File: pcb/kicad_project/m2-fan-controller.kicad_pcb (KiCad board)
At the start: 2 copper layers, 22 x 30 mm, 17 parts, among them J1 Bus_M.2_Socket_E, J2 Conn_01x04, J3 Conn_01x04, J4 JST PH_S2B-PH-K, U1 STM32F042F6P6

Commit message: Hopefully final revision
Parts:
- added TP1: TestPoint, TestPoint:TestPoint_Pad_D1.0mm, F.Cu at (138.5, 105.2)
- moved JP1 1.65 mm to (137.4, 86.5), turned to 180 degrees
- moved C1 0.41 mm to (144.5, 103.4)
- turned R7 to 0 degrees
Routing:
- net +3.3V: track 0.00 -> 40.5 mm, vias 0 -> 6
- net BOOT0: track 4.47 -> 21.7 mm
- net RST: track 0.00 -> 16.2 mm, vias 0 -> 2
- net TACH_1: track 0.00 -> 12.9 mm, vias 0 -> 2
- net TACH_0: track 0.00 -> 11.4 mm
- net PWM_0: track 0.00 -> 8.10 mm
- net PWM_1: track 0.00 -> 6.81 mm
- net Net-(J1-~{PERST0}): track 0.00 -> 5.77 mm, vias 0 -> 1
- net +12V: track 31.4 -> 27.5 mm
- net GND: track 0.00 -> 1.50 mm, vias 0 -> 4
- added copper zone on B.Cu, net +3.3V
- added copper zone on B.Cu, net GND
- added copper zone on F.Cu, net GND
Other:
- board text added: "(c) 2026 - Sergio Carmine"
- board text added: "3.3V"
- board text added: "M.2 fan controller"

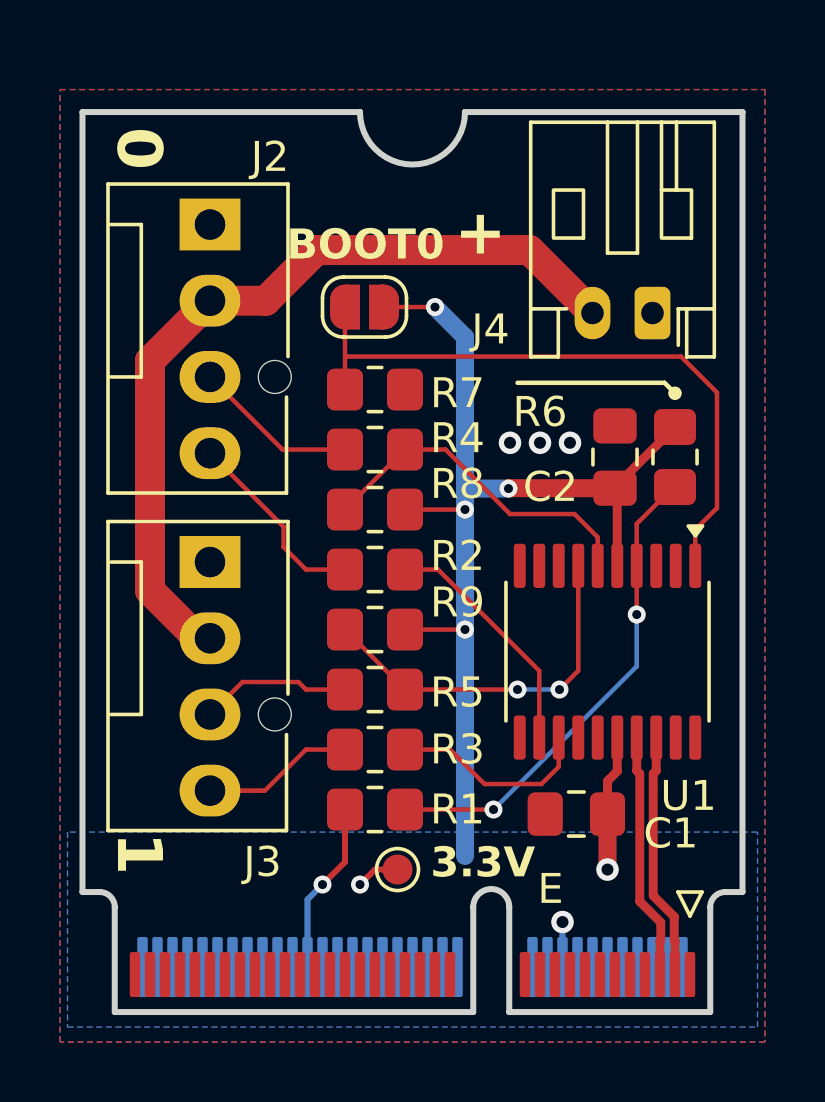
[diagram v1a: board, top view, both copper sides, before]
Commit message: Add debug header
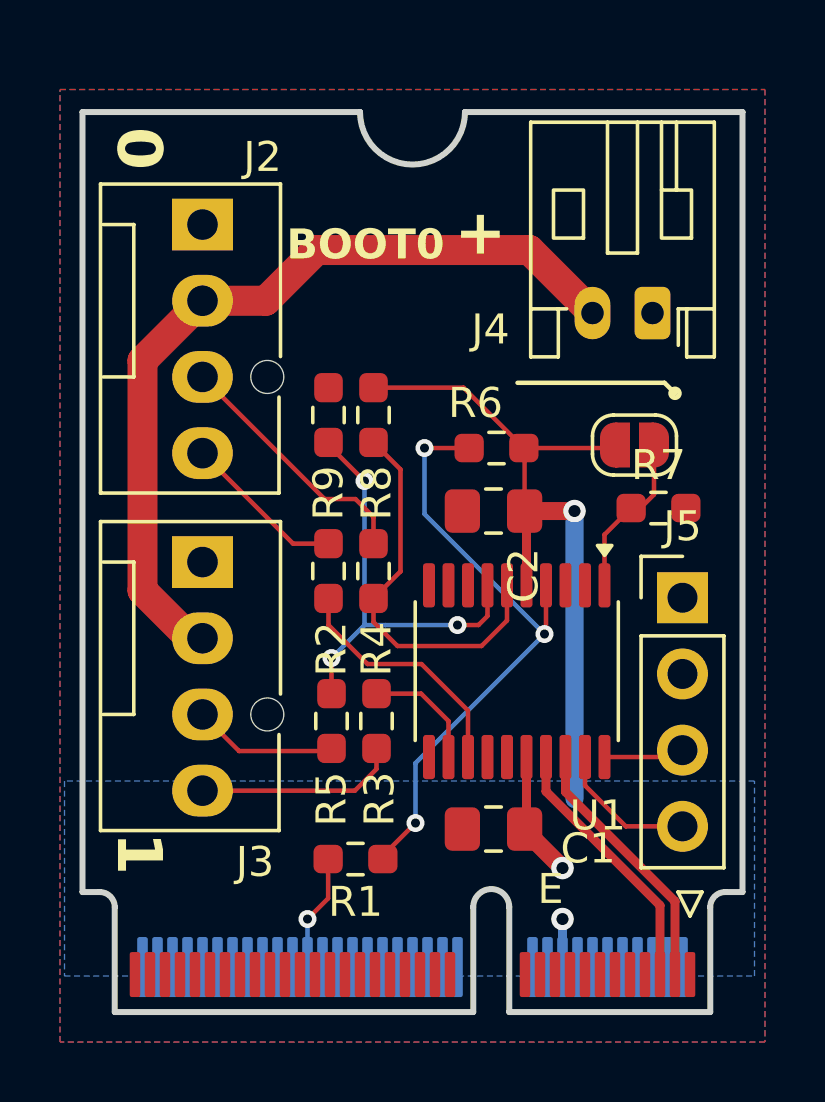
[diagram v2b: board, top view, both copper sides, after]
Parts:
- removed TP1: TestPoint, TestPoint:TestPoint_Pad_D1.0mm
- added J5: Conn_02x02_Odd_Even, Connector_PinHeader_2.54mm:PinHeader_1x04_P2.54mm_Vertical, F.Cu at (148.0, 96.2)
- R1, R2, R3, R4, R5, R6, R7, R8, R9: footprint Resistor_SMD:R_0805_2012Metric_Pad1.20x1.40mm_HandSolder -> Resistor_SMD:R_0603_1608Metric_Pad0.98x0.95mm_HandSolder
- moved R7 10.2 mm to (147.2, 93.2)
- moved JP1 10.1 mm to (146.4, 91.1), turned to 0 degrees
- moved R9 7.32 mm to (136.2, 90.1), turned to -90 degrees
- moved R6 5.96 mm to (141.8, 91.2), turned to 180 degrees
- moved C2 4.43 mm to (141.7, 93.3), turned to 180 degrees
- moved R4 4.05 mm to (137.7, 95.3), turned to 90 degrees
- moved R8 3.15 mm to (137.7, 90.1), turned to -90 degrees
- moved U1 3.09 mm to (142.5, 98.6)
- moved C1 2.81 mm to (141.7, 103.9)
- moved R5 1.79 mm to (136.3, 100.3), turned to -90 degrees
- moved R1 1.77 mm to (137.1, 104.9)
- moved R2 1.55 mm to (136.2, 95.3), turned to 90 degrees
- moved R3 0.95 mm to (137.8, 100.3), turned to -90 degrees
- moved J2 0.25 mm to (132.0, 83.8)
- moved J3 0.25 mm to (132.0, 95.0)
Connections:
- U1 pad 12: PWM_0 -> PWM_1
- U1 pad 13: PWM_1 -> PWM_0
- U1 pad 19: unconnected-(U1-PA13-Pad19) -> SWDIO
- U1 pad 20: unconnected-(U1-PA14-Pad20) -> SWCLK
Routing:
- net BOOT0: track 21.7 -> 5.94 mm
- net +3.3V: track 40.5 -> 29.1 mm, vias 6 -> 2
- net SWDIO: track 0.00 -> 4.76 mm
- net RST: track 16.2 -> 20.5 mm, vias 2 -> 3
- net Net-(J2-Pin_3): track 5.50 -> 8.55 mm
- net PWM_1: track 6.81 -> 3.98 mm
- net SWCLK: track 0.00 -> 2.70 mm
- net Net-(J1-~{PERST0}): track 5.77 -> 3.88 mm
- net TACH_1: track 12.9 -> 14.6 mm, vias 2 -> 3
- net Net-(J3-Pin_4): track 5.07 -> 6.79 mm
- net TACH_0: track 11.4 -> 13.0 mm
- net Net-(J2-Pin_4): track 6.51 -> 5.45 mm
- net Net-(J3-Pin_3): track 5.05 -> 4.31 mm
- net USB_D-: track 8.24 -> 8.82 mm
- net USB_D+: track 8.24 -> 8.76 mm
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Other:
- board text removed: "3.3V"

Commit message: Final revision
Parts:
- removed JP1: Jumper_2_Open, Jumper:SolderJumper-2_P1.3mm_Open_RoundedPad1.0x1.5mm
- added C3: 0.1uF, Capacitor_SMD:C_0805_2012Metric_Pad1.18x1.45mm_HandSolder, F.Cu at (136.6, 88.3)
- added C4: 0.1uF, Capacitor_SMD:C_0805_2012Metric_Pad1.18x1.45mm_HandSolder, F.Cu at (136.6, 93.9)
- added C5: 1uF, Capacitor_SMD:C_1206_3216Metric, F.Cu at (142.2, 88.8)
- added C6: 1uF, Capacitor_SMD:C_1206_3216Metric, F.Cu at (142.2, 91.2)
- added R10: 10kOhm, Resistor_SMD:R_0603_1608Metric_Pad0.98x0.95mm_HandSolder, F.Cu at (140.2, 103.0)
- added R11: 10kOhm, Resistor_SMD:R_0603_1608Metric_Pad0.98x0.95mm_HandSolder, F.Cu at (138.6, 103.0)
- added U2: TPS22810DBV, Package_TO_SOT_SMD:SOT-23-6, F.Cu at (136.7, 85.6)
- added U3: TPS22810DBV, Package_TO_SOT_SMD:SOT-23-6, F.Cu at (136.7, 91.2)
- C1, C2: footprint Capacitor_SMD:C_0805_2012Metric_Pad1.18x1.45mm_HandSolder -> Capacitor_SMD:C_0603_1608Metric_Pad1.08x0.95mm_HandSolder
- J2, J3: value Conn_01x04 -> JST PH_B4B-PH-K; footprint Connector:FanPinHeader_1x04_P2.54mm_Vertical -> Connector_JST:JST_PH_B4B-PH-K_1x04_P2.00mm_Vertical
- J4: footprint Connector_JST:JST_PH_S2B-PH-K_1x02_P2.00mm_Horizontal -> Connector_JST:JST_PH_B2B-PH-K_1x02_P2.00mm_Vertical
- J5: footprint Connector_PinHeader_2.54mm:PinHeader_1x04_P2.54mm_Vertical -> Connector_PinHeader_1.27mm:PinHeader_1x05_P1.27mm_Vertical
- moved R8 13.1 mm to (135.4, 103.0), turned to 90 degrees
- moved R9 12.9 mm to (137.0, 103.0), turned to 90 degrees
- moved J5 7.00 mm to (148.1, 89.2)
- moved J2 6.80 mm to (130.6, 90.4), turned to 90 degrees
- moved J3 6.55 mm to (130.6, 101.4), turned to 90 degrees
- moved R7 5.15 mm to (145.5, 88.3), turned to 90 degrees
- moved R5 4.75 mm to (140.2, 97.6), turned to 90 degrees
- moved J4 4.38 mm to (145.1, 82.8), turned to 0 degrees
- moved R1 4.35 mm to (132.8, 104.9)
- moved R6 3.87 mm to (145.5, 92.3), turned to -90 degrees
- moved R3 3.62 mm to (135.4, 97.6), turned to 90 degrees
- moved U1 3.18 mm to (145.4, 99.9)
- moved C1 3.00 mm to (144.6, 104.8)
- moved C2 2.62 mm to (143.6, 95.1)
- moved R4 2.46 mm to (138.6, 97.6)
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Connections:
- J2 pad 2: +12V -> Net-(J2-Pin_2)
- J3 pad 2: +12V -> Net-(J3-Pin_2)
- J5 pad 2: +3.3V -> SWCLK
- J5 pad 3: SWCLK -> SWDIO
- J5 pad 4: SWDIO -> BOOT0
- U1 pad 8: unconnected-(U1-PA2-Pad8) -> EN_0
- U1 pad 9: unconnected-(U1-PA3-Pad9) -> EN_1
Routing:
- net EN_0: track 0.00 -> 24.8 mm, vias 0 -> 3
- net EN_1: track 0.00 -> 19.4 mm, vias 0 -> 3
- net Net-(J2-Pin_4): track 5.45 -> 17.2 mm, vias 0 -> 1
- net Net-(J3-Pin_2): track 0.00 -> 11.2 mm
- net SWCLK: track 2.70 -> 13.4 mm, vias 0 -> 1
- net Net-(J2-Pin_3): track 8.55 -> 17.1 mm, vias 0 -> 1
- net +12V: track 27.6 -> 19.9 mm
- net Net-(J2-Pin_2): track 0.00 -> 7.45 mm
- net SWDIO: track 4.76 -> 12.0 mm, vias 0 -> 1
- net PWM_1: track 3.98 -> 11.1 mm
- net GND: track 1.60 -> 7.94 mm, vias 1 -> 11
- net Net-(J3-Pin_3): track 4.31 -> 10.1 mm, vias 0 -> 1
- net BOOT0: track 5.94 -> 10.0 mm
- net Net-(J1-~{PERST0}): track 3.88 -> 6.62 mm
- net USB_D-: track 8.82 -> 6.34 mm
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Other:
- board text added: "12V"
- board text added: "3.3V"
- board text added: "G"
- board text added: "GND"
- board text added: "PCB thickness 0.8 mm"
- board text added: "PWM"
- board text added: "SWCLK"
- board text added: "SWDIO"
- board text added: "TACH"
- board text removed: "+"
- board text removed: "M.2 fan controller"

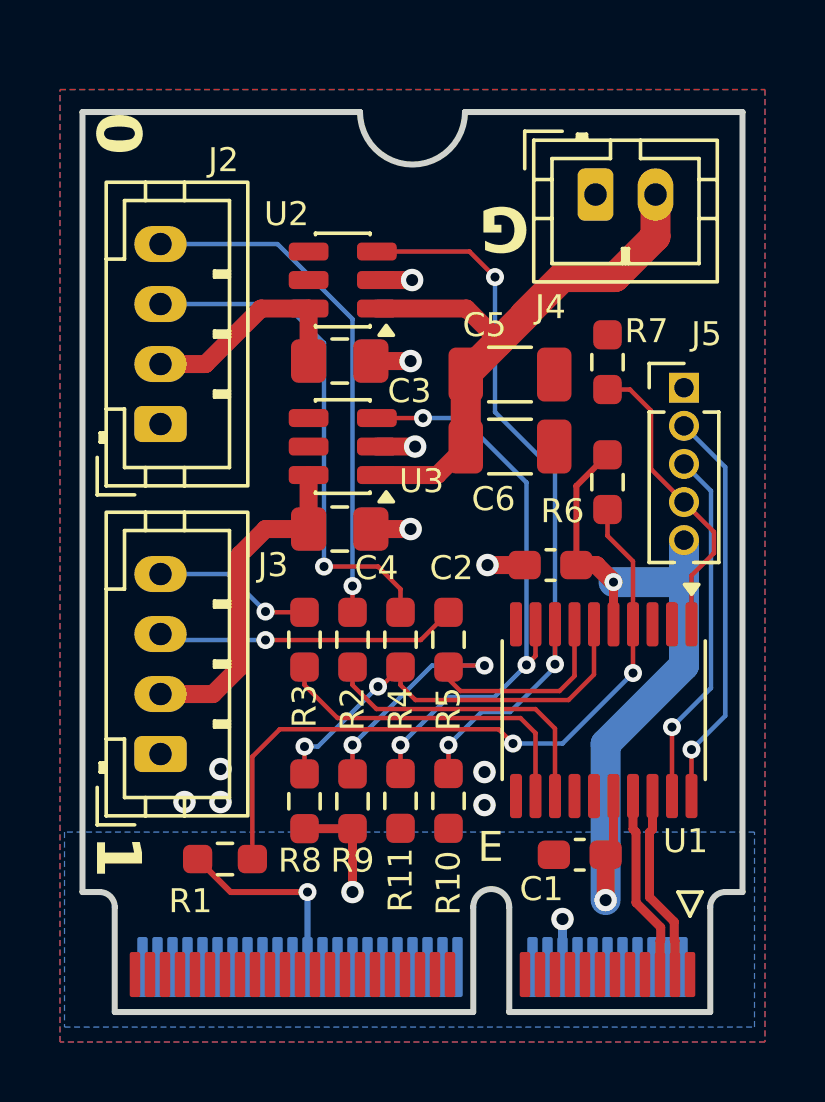
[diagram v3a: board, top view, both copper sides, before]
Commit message: Use 0603 components
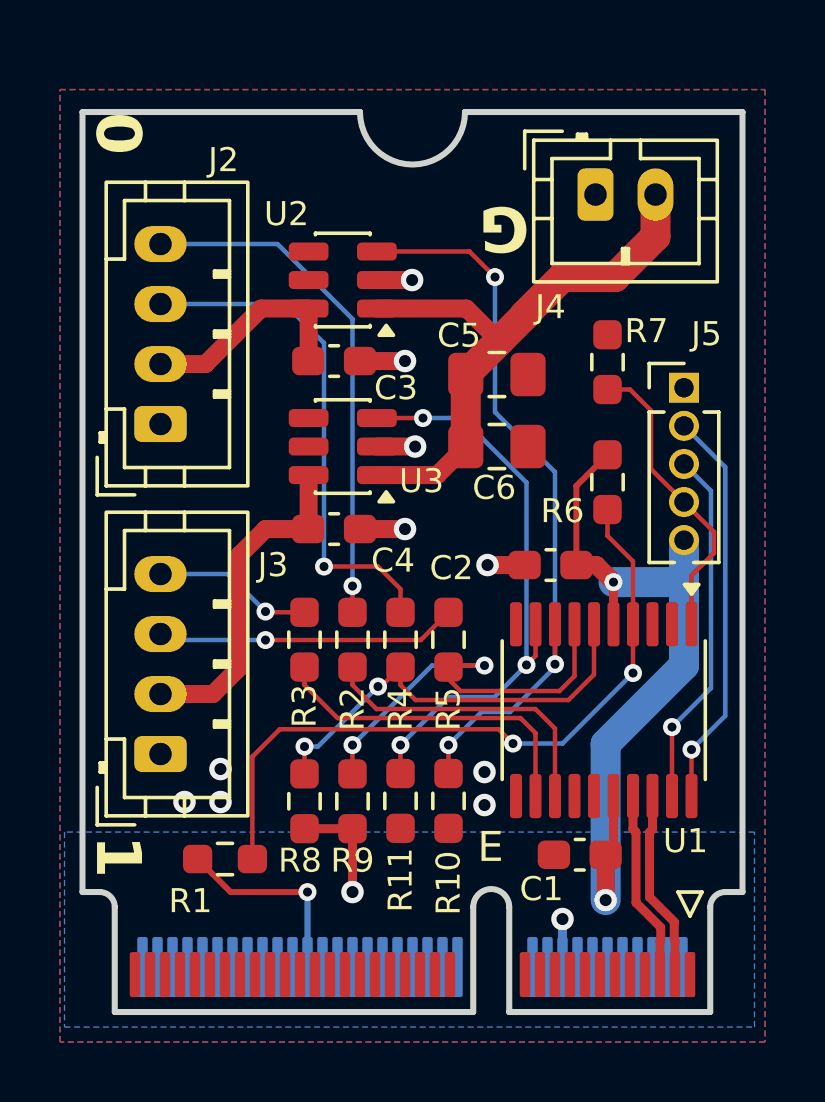
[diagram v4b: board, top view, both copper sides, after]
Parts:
- C3, C4: footprint Capacitor_SMD:C_0805_2012Metric_Pad1.18x1.45mm_HandSolder -> Capacitor_SMD:C_0603_1608Metric_Pad1.08x0.95mm_HandSolder
- C5, C6: footprint Capacitor_SMD:C_1206_3216Metric -> Capacitor_SMD:C_0805_2012Metric_Pad1.18x1.45mm_HandSolder
- moved C5 0.44 mm to (141.8, 88.8)
- moved C6 0.44 mm to (141.8, 91.2)
- moved C3 0.19 mm to (136.4, 88.3)
- moved C4 0.19 mm to (136.4, 93.9)
